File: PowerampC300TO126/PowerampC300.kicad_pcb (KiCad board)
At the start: 2 copper layers, 240 x 63 mm, 127 parts, among them J1 Conn_01x02, J2 Conn_01x02, J3 Conn_01x02, J4 Conn_01x01, J5 Conn_01x01, J6 Conn_01x01, J7 Conn_01x01, J8 Conn_01x02, J9 Conn_Coaxial, Q1 2N5551, Q10 MJE350, Q11 MJE340, Q12 MJE340, Q13 2N5551, Q14 2N5401, Q15 MJE340, Q16 MJE350, Q17 MJL3281A, Q18 MJL1302A, Q19 MJL3281A, Q2 2N5551, Q20 MJL1302A, Q21 MJL3281A, Q22 MJL1302A, Q23 MJL3281A, Q24 MJL1302A, Q3 2N5401, Q4 2N5401, Q5 2N5551, Q6 2N5551, Q7 2N5551, Q8 2N5401, U1 MOC3020M

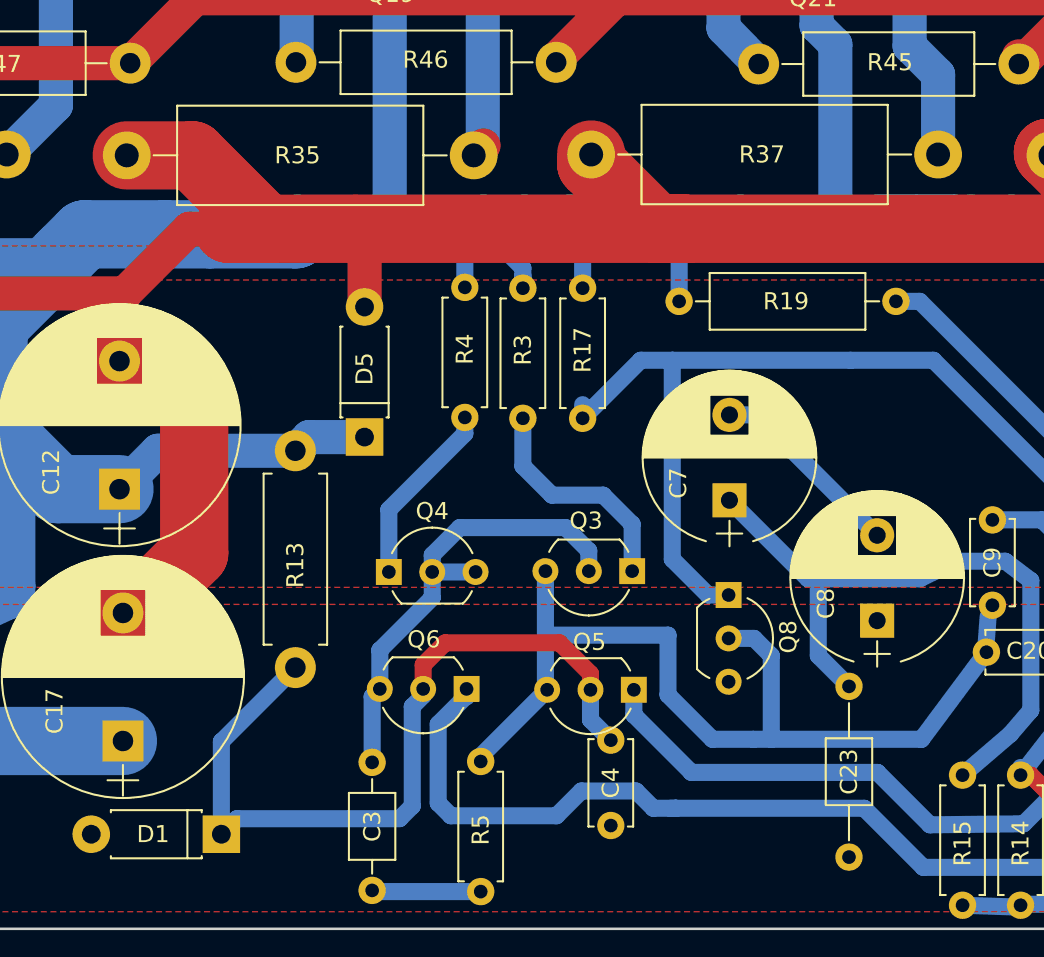
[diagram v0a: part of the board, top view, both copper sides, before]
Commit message: Added back Q9 transistor for Q8 protection
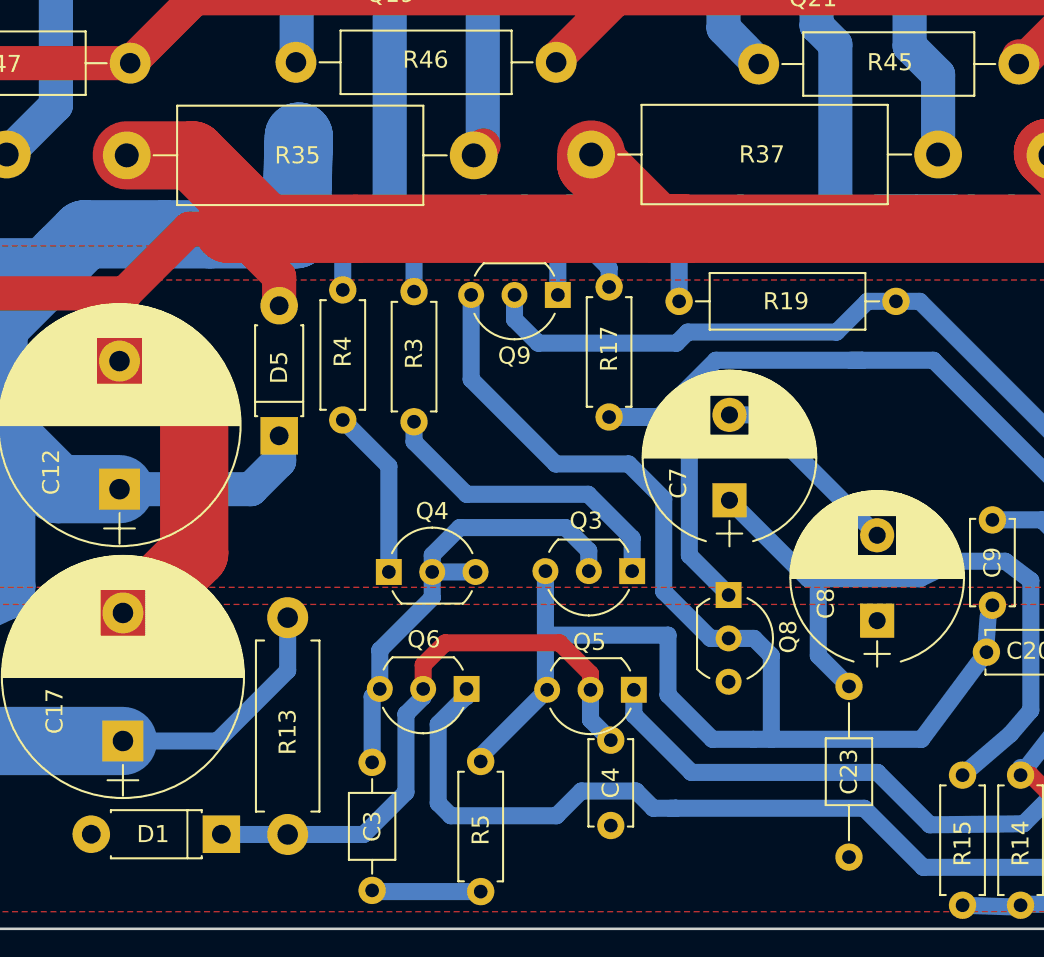
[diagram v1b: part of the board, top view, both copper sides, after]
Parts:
- added Q9: 2N5401, TO_SOT_Packages_THT:TO-92_Inline_Wide, F.Cu at (80.3, 68.9)
- moved R13 9.79 mm to (64.5, 100.5)
- moved R4 7.15 mm to (67.7, 76.2)
- moved R3 6.38 mm to (71.9, 76.3)
- moved D5 5.00 mm to (64.0, 77.1)
- moved R17 1.55 mm to (83.3, 76.0)
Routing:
- net +48V: track 336.1 -> 367.1 mm
- net Net-(C20-Pad1): track 56.3 -> 85.8 mm
- net Net-(Q10-Pad1): track 23.4 -> 48.8 mm
- net Net-(C4-Pad2): track 47.5 -> 35.2 mm
- net Net-(Q3-Pad1): track 13.4 -> 18.2 mm
- net Net-(Q10-Pad3): track 66.7 -> 64.3 mm
- net Net-(Q4-Pad1): track 10.9 -> 10.0 mm
- net Net-(C20-Pad2): track 503.1 -> 504.0 mm
